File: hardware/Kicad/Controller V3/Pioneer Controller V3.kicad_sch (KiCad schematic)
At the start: 23 parts, among them J1 Sensor Connector, J2 Power (IN), J4 Conn_Coaxial, SW1 SW_Push, SW2 SW_Push, SW5 SW_DIP_x02, U1 ESP32-S3, U2 2821, U3 DS3231_Precision_RTC, U4 RFM95W_LoRa_Radio_Transceiver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

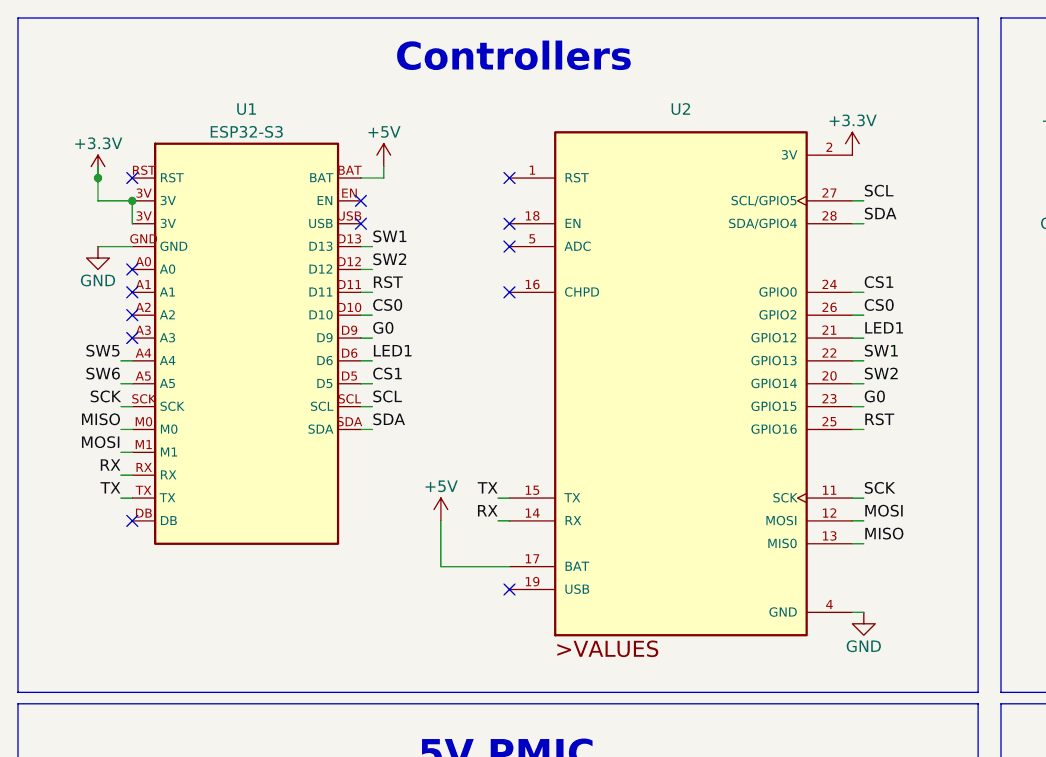
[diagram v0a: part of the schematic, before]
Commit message: updated 5v
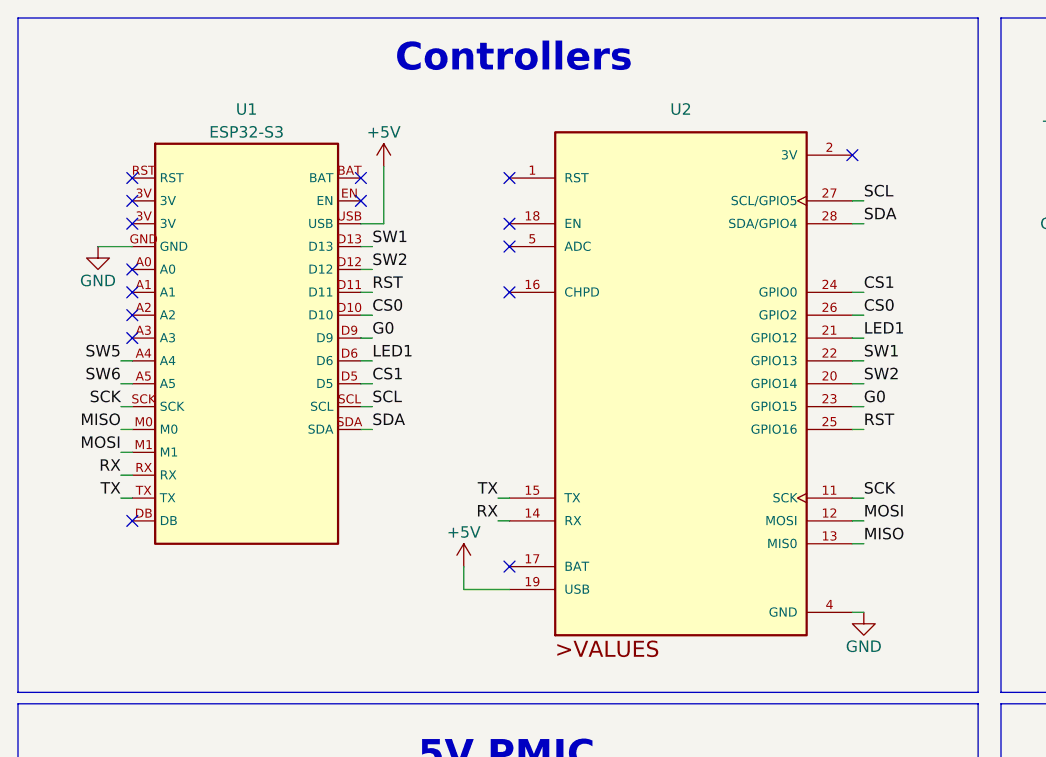
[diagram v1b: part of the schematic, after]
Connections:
- net +5V: now also U1.USB, U2.19 (USB); no longer U1.BAT, U2.17 (BAT)
- net +3V3: no longer names the net of U1.3V
- net +3V3: no longer U2.2 (3V)
- no-connect marks 26 -> 29
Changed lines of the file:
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@@
   (junction (at 35.56 111.76) (diameter 0) (color 0 0 0 0)
   )
-  (junction (at 25.4 33.02) (diameter 0) (color 0 0 0 0)
-  )
   (junction (at 88.9 130.81) (diameter 0) (color 0 0 0 0)
   )
@@
   )
   (junction (at 234.95 72.39) (diameter 0) (color 0 0 0 0)
-  )
-  (junction (at 21.59 30.48) (diameter 0) (color 0 0 0 0)
   )
   (junction (at 102.87 111.76) (diameter 0) (color 0 0 0 0)
@@
   (no_connect (at 190.5 39.37))
   (no_connect (at 149.86 78.74))
+  (no_connect (at 67.31 73.66))
   (no_connect (at 25.4 45.72))
   (no_connect (at 25.4 48.26))
   (no_connect (at 25.4 68.58))
   (no_connect (at 50.8 33.02))
-  (no_connect (at 50.8 35.56))
   (no_connect (at 157.48 31.75))
   (no_connect (at 157.48 29.21))
@@
   (no_connect (at 157.48 39.37))
   (no_connect (at 157.48 34.29))
+  (no_connect (at 25.4 33.02))
   (no_connect (at 67.31 30.48))
   (no_connect (at 67.31 35.56))
   (no_connect (at 67.31 38.1))
   (no_connect (at 67.31 43.18))
-  (no_connect (at 67.31 76.2))
   (no_connect (at 25.4 40.64))
   (no_connect (at 25.4 43.18))
+  (no_connect (at 25.4 35.56))
+  (no_connect (at 50.8 30.48))
   (no_connect (at 148.59 114.3))
   (no_connect (at 25.4 30.48))
+  (no_connect (at 105.41 27.94))
   (no_connect (at 134.62 34.29))
   (polyline (pts (xy 203.2 87.63) (xy 203.2 12.7))
@@
     (stroke (width 0) (type default))
   )
-  (wire (pts (xy 59.69 68.58) (xy 59.69 73.66))
+  (wire (pts (xy 67.31 76.2) (xy 62.23 76.2))
+    (stroke (width 0) (type default))
+  )
+  (wire (pts (xy 62.23 73.66) (xy 62.23 76.2))
     (stroke (width 0) (type default))
   )
@@
     (stroke (width 0) (type default))
   )
+  (wire (pts (xy 53.34 29.21) (xy 53.34 35.56))
+    (stroke (width 0) (type default))
+  )
   (wire (pts (xy 151.13 71.12) (xy 149.86 71.12))
     (stroke (width 0) (type default))
@@
     (stroke (width 0) (type default))
   )
-  (wire (pts (xy 25.4 33.02) (xy 21.59 33.02))
-    (stroke (width 0) (type default))
-  )
   (wire (pts (xy 256.54 72.39) (xy 251.46 72.39))
     (stroke (width 0) (type default))
@@
     (stroke (width 0) (type default))
   )
-  (wire (pts (xy 21.59 29.21) (xy 21.59 30.48))
-    (stroke (width 0) (type default))
-  )
   (wire (pts (xy 52.07 38.1) (xy 50.8 38.1))
     (stroke (width 0) (type default))
@@
     (stroke (width 0) (type default))
   )
-  (wire (pts (xy 50.8 30.48) (xy 53.34 30.48))
-    (stroke (width 0) (type default))
-  )
-  (wire (pts (xy 21.59 30.48) (xy 21.59 33.02))
-    (stroke (width 0) (type default))
-  )
   (wire (pts (xy 52.07 45.72) (xy 50.8 45.72))
     (stroke (width 0) (type default))
@@
     (stroke (width 0) (type default))
   )
-  (wire (pts (xy 53.34 30.48) (xy 53.34 29.21))
-    (stroke (width 0) (type default))
-  )
   (polyline (pts (xy 205.74 106.68) (xy 284.48 106.68))
     (stroke (width 0) (type default))
@@
     (stroke (width 0) (type default))
   )
-  (wire (pts (xy 25.4 33.02) (xy 25.4 35.56))
-    (stroke (width 0) (type default))
-  )
   (wire (pts (xy 196.85 31.75) (xy 196.85 38.1))
     (stroke (width 0) (type default))
@@
     (stroke (width 0) (type default))
   )
+  (wire (pts (xy 50.8 35.56) (xy 53.34 35.56))
+    (stroke (width 0) (type default))
+  )
   (wire (pts (xy 106.68 55.88) (xy 105.41 55.88))
     (stroke (width 0) (type default))
@@
   )
   (wire (pts (xy 60.96 120.65) (xy 64.77 120.65))
-    (stroke (width 0) (type default))
-  )
-  (wire (pts (xy 59.69 73.66) (xy 67.31 73.66))
     (stroke (width 0) (type default))
   )
@@
         (path "/928ded6b-90e0-41cf-9552-9c708ef4c4d3"
           (reference "J4") (unit 1)
-        )
-      )
-    )
-  )
-  (symbol (lib_id "power:+3.3V") (at 21.59 30.48 0) (unit 1)
-    (in_bom yes) (on_board yes) (dnp no)
-    (property "Reference" "#PWR0110" (at 21.59 34.29 0)
-      (effects (font (size 1.27 1.27)) hide)
-    )
-    (property "Value" "+3.3V" (at 21.59 26.67 0)
-      (effects (font (size 1.27 1.27)))
-    )
-    (property "Footprint" "" (at 21.59 30.48 0)
-      (effects (font (size 1.27 1.27)) hide)
-    )
-    (property "Datasheet" "" (at 21.59 30.48 0)
-      (effects (font (size 1.27 1.27)) hide)
-    )
-    (pin "1")
-    (instances
-      (project "Pioneer Controller V3"
-        (path "/928ded6b-90e0-41cf-9552-9c708ef4c4d3"
-          (reference "#PWR0110") (unit 1)
         )
       )
@@
     )
   )
-  (symbol (lib_id "power:+3.3V") (at 105.41 27.94 0) (unit 1)
-    (in_bom yes) (on_board yes) (dnp no)
-    (property "Reference" "#PWR0118" (at 105.41 31.75 0)
-      (effects (font (size 1.27 1.27)) hide)
-    )
-    (property "Value" "+3.3V" (at 105.41 24.13 0)
-      (effects (font (size 1.27 1.27)))
-    )
-    (property "Footprint" "" (at 105.41 27.94 0)
-      (effects (font (size 1.27 1.27)) hide)
-    )
-    (property "Datasheet" "" (at 105.41 27.94 0)
-      (effects (font (size 1.27 1.27)) hide)
-    )
-    (pin "1")
-    (instances
-      (project "Pioneer Controller V3"
-        (path "/928ded6b-90e0-41cf-9552-9c708ef4c4d3"
-          (reference "#PWR0118") (unit 1)
-        )
-      )
-    )
-  )
   (symbol (lib_id "Adafruit_HUZZAH_ESP8266_Basic_Breakout-eagle-import:VIN") (at 26.67 105.41 0) (unit 1)
     (in_bom yes) (on_board yes) (dnp no) (fields_autoplaced)
@@
     )
   )
-  (symbol (lib_id "power:+5V") (at 59.69 68.58 0) (unit 1)
-    (in_bom yes) (on_board yes) (dnp no)
-    (property "Reference" "#PWR05" (at 59.69 72.39 0)
-      (effects (font (size 1.27 1.27)) hide)
-    )
-    (property "Value" "+5V" (at 59.69 64.77 0)
-      (effects (font (size 1.27 1.27)))
-    )
-    (property "Footprint" "" (at 59.69 68.58 0)
-      (effects (font (size 1.27 1.27)) hide)
-    )
-    (property "Datasheet" "" (at 59.69 68.58 0)
-      (effects (font (size 1.27 1.27)) hide)
-    )
+  (symbol (lib_id "power:+5V") (at 62.23 73.66 0) (unit 1)
+    (in_bom yes) (on_board yes) (dnp no)
+    (property "Reference" "#PWR05" (at 62.23 77.47 0)
+      (effects (font (size 1.27 1.27)) hide)
+    )
+    (property "Value" "+5V" (at 62.23 69.85 0)
+      (effects (font (size 1.27 1.27)))
+    )
+    (property "Footprint" "" (at 62.23 73.66 0)
+      (effects (font (size 1.27 1.27)) hide)
+    )
+    (property "Datasheet" "" (at 62.23 73.66 0)
+      (effects (font (size 1.27 1.27)) hide)
+    )
